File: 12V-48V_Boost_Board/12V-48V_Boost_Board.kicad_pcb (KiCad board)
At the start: 2 copper layers, 65.1 x 76.7 mm, 39 parts, among them J1 12V Input, J2 Input Current Sensing, J3 Output Current Sensing, J4 48V Output, J5 Output Measuring, Q1 FDWS86068-F085

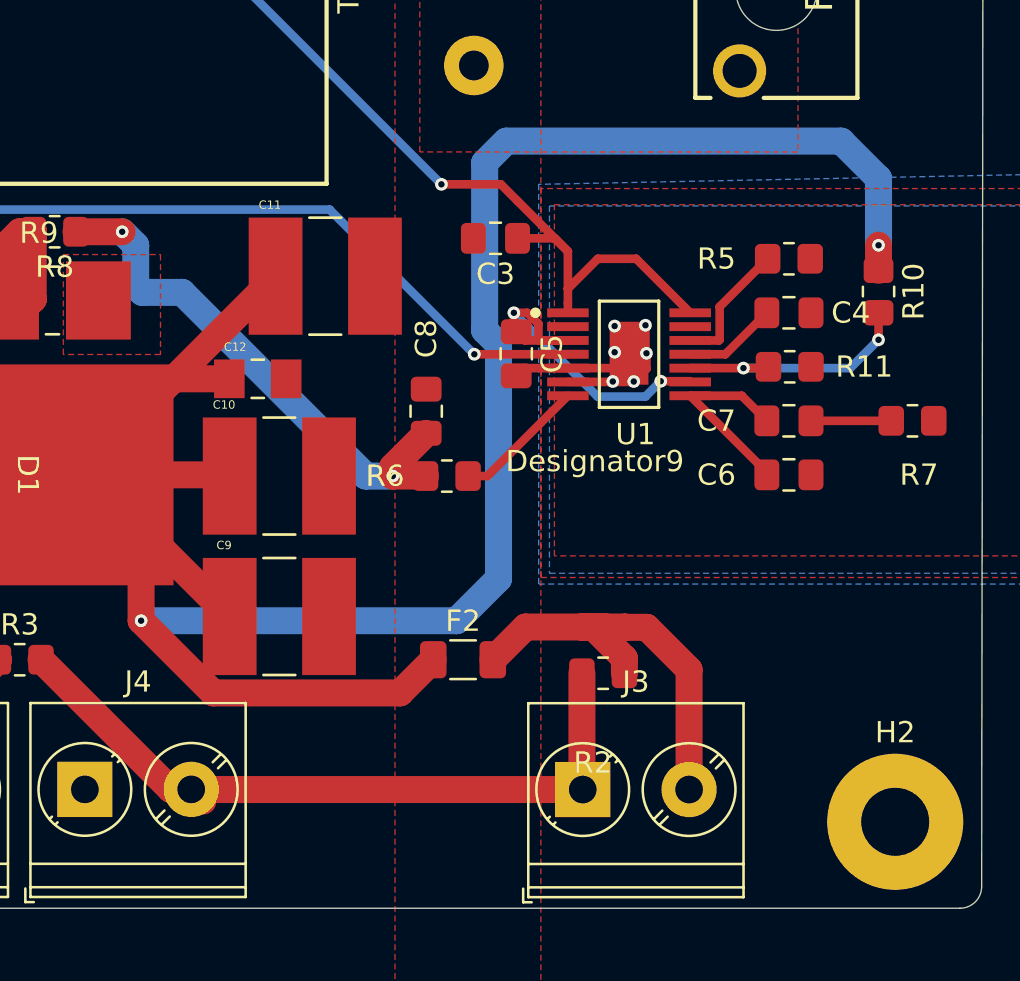
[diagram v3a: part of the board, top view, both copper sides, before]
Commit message: Added opamp
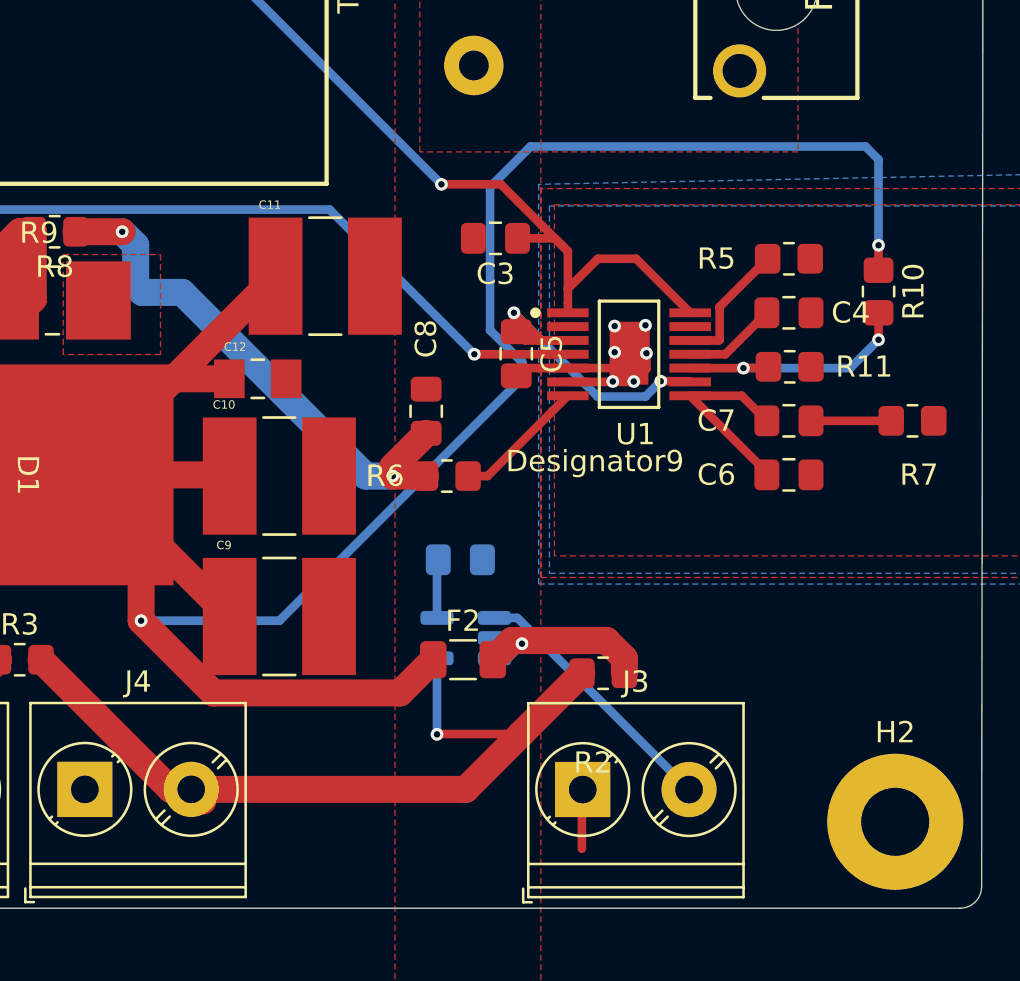
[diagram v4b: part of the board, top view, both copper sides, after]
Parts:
- added C13: 0.1uF, Capacitor_SMD:C_0805_2012Metric_Pad1.18x1.45mm_HandSolder, B.Cu at (147.2, 128.4)
- added H5: Logo, 12/48 boost:Logo_SilkScreen_10mm, B.Cu at (112.5, 93.6)
- added U2: INA180, Package_TO_SOT_SMD:SOT-23-5_HandSoldering, B.Cu at (147.4, 132.1)
- R2: value 1mΩ -> 25mΩ
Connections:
- F2 pad 2: Net-(J3-Pin_2) -> Net-(U2-IN+)
- J3 pad 1: Net-(J3-Pin_1) -> GND
- J4 pad 2: Net-(J3-Pin_1) -> Net-(J4-Pin_2)
- R2 pad 1: Net-(J3-Pin_2) -> Net-(U2-IN+)
- R2 pad 2: Net-(J3-Pin_1) -> Net-(J4-Pin_2)
- R3 pad 2: Net-(J3-Pin_1) -> Net-(J4-Pin_2)
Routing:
- net Net-(J4-Pin_2): track 0.00 -> 38.5 mm, vias 0 -> 1
- net Net-(J3-Pin_1): track 34.3 -> 0.00 mm
- net Net-(U2-IN+): track 0.00 -> 10.9 mm, vias 0 -> 1
- net Net-(J3-Pin_2): track 20.8 -> 13.1 mm
- net /Boost_Board_Chip/48V_OUTPUT: track 125.2 -> 120.6 mm
- net GND: track 16.5 -> 19.4 mm
- net +5V: track 0.00 -> 2.76 mm
- net /Boost_Board_Chip/DITHOFF: track 17.3 -> 18.2 mm
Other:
- board text added: "12V-48V BOOST BOARD KOBY SEELIGSOHN"

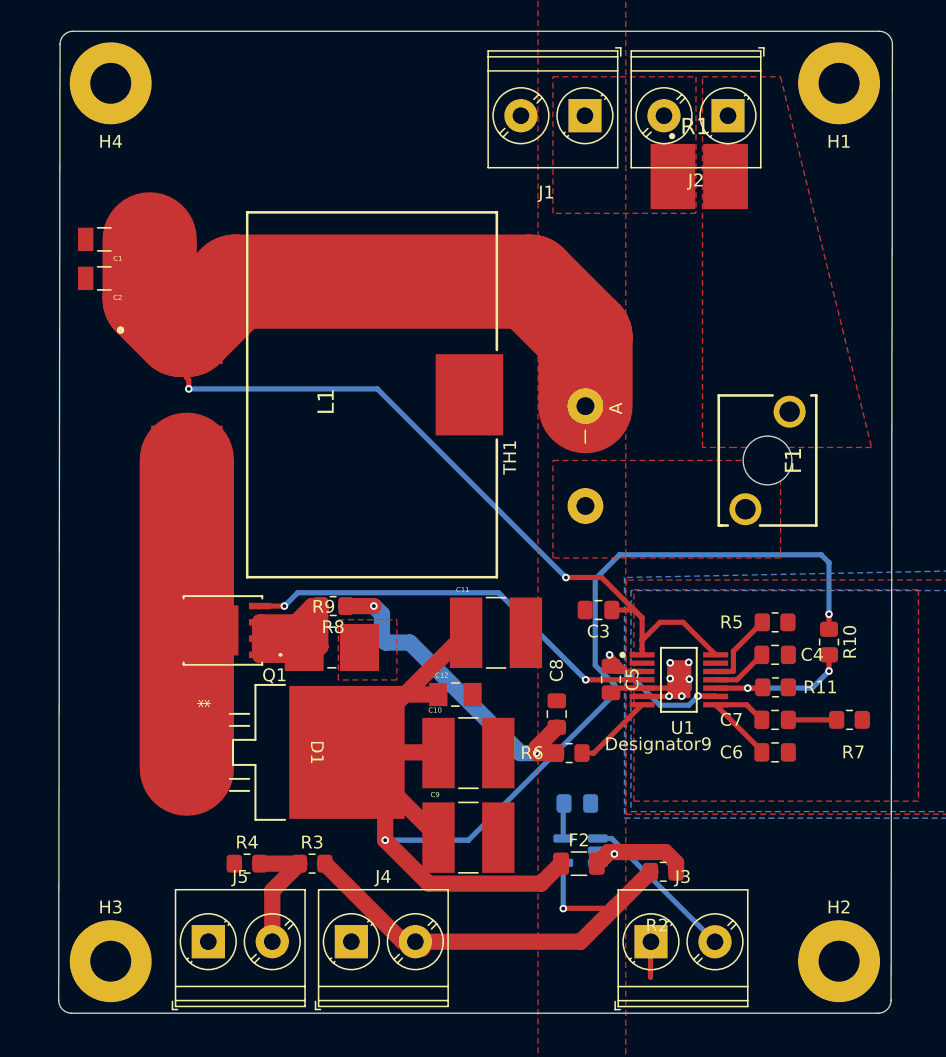
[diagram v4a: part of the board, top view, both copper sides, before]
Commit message: Changed silkscreen and vias
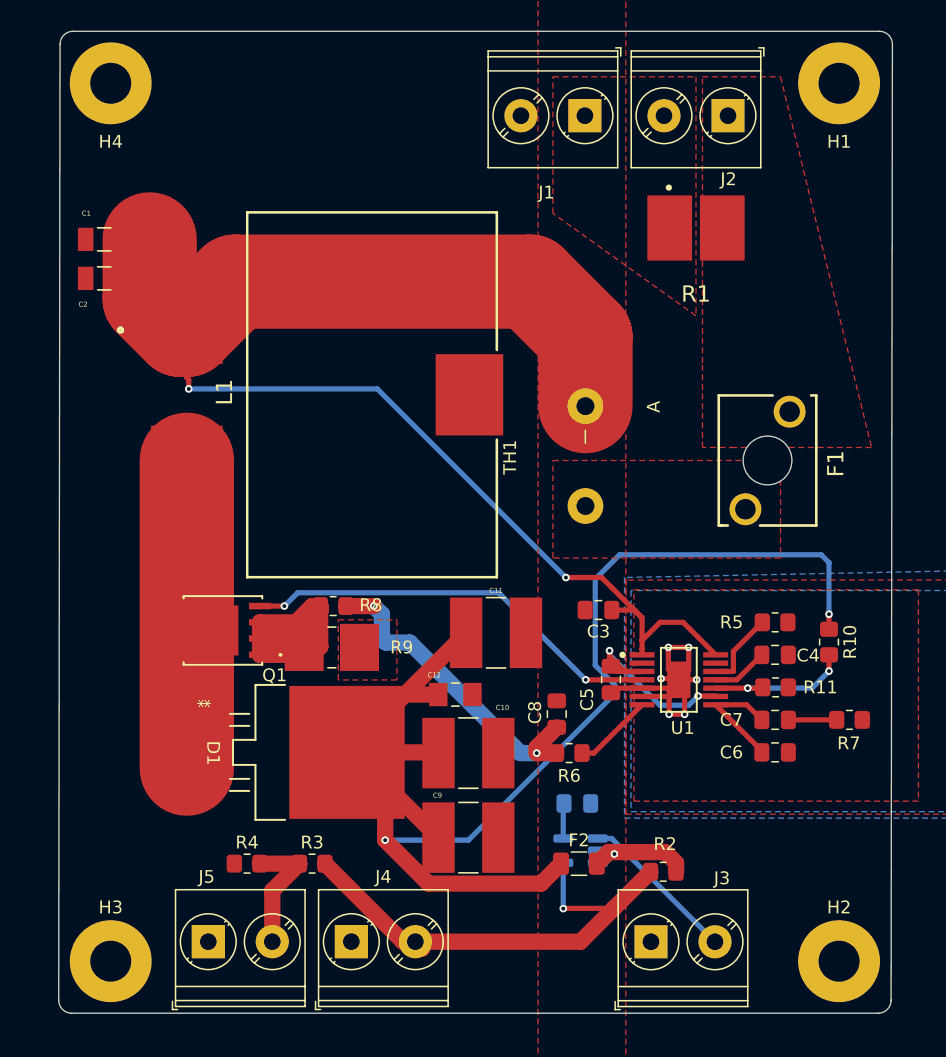
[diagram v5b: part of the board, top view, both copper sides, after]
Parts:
- moved R1 4.03 mm to (156.5, 83.4)
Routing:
- net GND: track 19.4 -> 23.8 mm

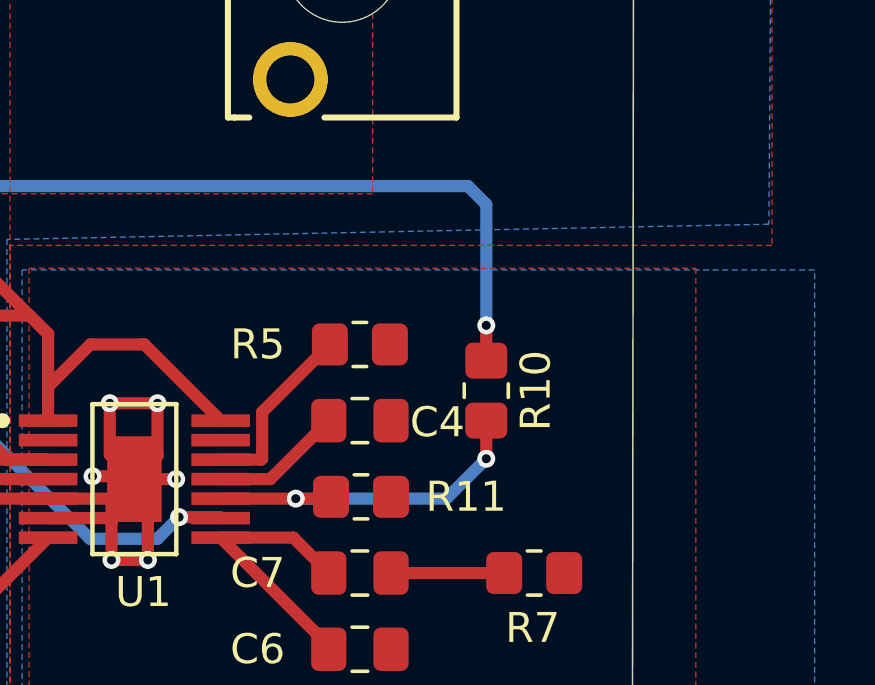
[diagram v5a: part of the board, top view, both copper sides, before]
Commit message: Changed 63nF cap footprint
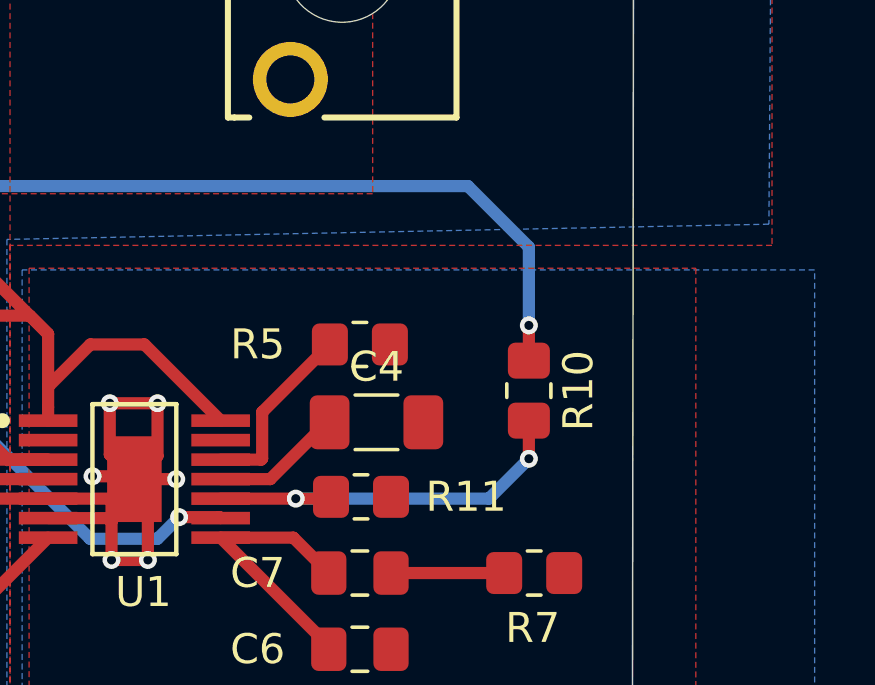
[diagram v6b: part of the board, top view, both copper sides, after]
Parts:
- C4: footprint Capacitor_SMD:C_0805_2012Metric_Pad1.18x1.45mm_HandSolder -> Capacitor_SMD:C_1206_3216Metric_Pad1.33x1.80mm_HandSolder
- F1: value 15A -> 12A
- U2: value INA180 -> INA290
- moved R10 1.42 mm to (168.3, 115.8)
- moved C4 0.56 mm to (163.2, 116.8)
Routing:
- net Net-(U1-FB): track 11.8 -> 13.2 mm
- net /Boost_Board_Chip/48V_OUTPUT: track 120.6 -> 121.1 mm
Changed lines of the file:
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@@
 			)
 		)
-		(property "Description" "08053C104KAT2A"
+		(property "Description" "CKG57NX7R2A106M500JH"
 			(at 0 0 0)
 			(layer "F.Fab")
@@
 			)
 		)
-		(property "Description" "08053C104KAT2A"
+		(property "Description" "CKG57NX7R2A106M500JH"
 			(at 0 0 0)
 			(layer "F.Fab")
@@
 			)
 		)
-		(property "Description" "08053C104KAT2A"
+		(property "Description" "CKG57NX7R2A106M500JH"
 			(at 0 0 0)
 			(layer "F.Fab")
@@
 			)
 		)
-		(property "Description" "Unpolarized capacitor"
+		(property "Description" "C3216X7R2A105M160AA"
 			(at 0 0 0)
 			(layer "F.Fab")
@@
 		)
 	)
-	(footprint "Capacitor_SMD:C_0805_2012Metric_Pad1.18x1.45mm_HandSolder"
+	(footprint "Capacitor_SMD:C_1206_3216Metric_Pad1.33x1.80mm_HandSolder"
 		(layer "F.Cu")
-		(at 162.642502 116.7842)
-		(descr "Capacitor SMD 0805 (2012 Metric), square (rectangular) end terminal, IPC_7351 nominal with elongated pad for handsoldering. (Body size source: IPC-SM-782 page 76, https://www.pcb-3d.com/wordpress/wp-content/uploads/ipc-sm-782a_amendment_1_and_2.pdf, https://docs.google.com/spreadsheets/d/1BsfQQcO9C6DZCsRaXUlFlo91Tg2WpOkGARC1WS5S8t0/edit?usp=sharing), generated with kicad-footprint-generator")
+		(at 163.195 116.84)
+		(descr "Capacitor SMD 1206 (3216 Metric), square (rectangular) end terminal, IPC_7351 nominal with elongated pad for handsoldering. (Body size source: IPC-SM-782 page 76, https://www.pcb-3d.com/wordpress/wp-content/uploads/ipc-sm-782a_amendment_1_and_2.pdf), generated with kicad-footprint-generator")
 		(tags "capacitor handsolder")
 		(property "Reference" "C4"
-			(at 2.584498 0.0558 0)
+			(at 0 -1.85 0)
 			(layer "F.SilkS")
 			(effects
@@
 		)
 		(property "Value" "63nF"
-			(at 0.2755 1.981851 0)
+			(at 0 1.85 0)
 			(layer "F.Fab")
 			(effects
@@
 			)
 		)
-		(property "Footprint" "Capacitor_SMD:C_0805_2012Metric_Pad1.18x1.45mm_HandSolder"
+		(property "Footprint" "Capacitor_SMD:C_1206_3216Metric_Pad1.33x1.80mm_HandSolder"
 			(at 0 0 0)
 			(unlocked yes)
@@
 		(attr smd)
 		(fp_line
-			(start -0.261252 -0.735)
-			(end 0.261252 -0.735)
+			(start -0.711252 -0.91)
+			(end 0.711252 -0.91)
 			(stroke
 				(width 0.12)
@@
 		)
 		(fp_line
-			(start -0.261252 0.735)
-			(end 0.261252 0.735)
+			(start -0.711252 0.91)
+			(end 0.711252 0.91)
 			(stroke
 				(width 0.12)
@@
 		)
 		(fp_line
-			(start -1.88 -0.98)
-			(end 1.88 -0.98)
+			(start -2.48 -1.15)
+			(end 2.48 -1.15)
 			(stroke
 				(width 0.05)
@@
 		)
 		(fp_line
-			(start -1.88 0.98)
-			(end -1.88 -0.98)
+			(start -2.48 1.15)
+			(end -2.48 -1.15)
 			(stroke
 				(width 0.05)
@@
 		)
 		(fp_line
-			(start 1.88 -0.98)
-			(end 1.88 0.98)
+			(start 2.48 -1.15)
+			(end 2.48 1.15)
 			(stroke
 				(width 0.05)
@@
 		)
 		(fp_line
-			(start 1.88 0.98)
-			(end -1.88 0.98)
+			(start 2.48 1.15)
+			(end -2.48 1.15)
 			(stroke
 				(width 0.05)
@@
 		)
 		(fp_line
-			(start -1 -0.625)
-			(end 1 -0.625)
+			(start -1.6 -0.8)
+			(end 1.6 -0.8)
 			(stroke
 				(width 0.1)
@@
 		)
 		(fp_line
-			(start -1 0.625)
-			(end -1 -0.625)
+			(start -1.6 0.8)
+			(end -1.6 -0.8)
 			(stroke
 				(width 0.1)
@@
 		)
 		(fp_line
-			(start 1 -0.625)
-			(end 1 0.625)
+			(start 1.6 -0.8)
+			(end 1.6 0.8)
 			(stroke
 				(width 0.1)
@@
 		)
 		(fp_line
-			(start 1 0.625)
-			(end -1 0.625)
+			(start 1.6 0.8)
+			(end -1.6 0.8)
 			(stroke
 				(width 0.1)
@@
 			(effects
 				(font
-					(size 0.5 0.5)
-					(thickness 0.08)
+					(size 0.8 0.8)
+					(thickness 0.12)
 				)
 			)
 		)
 		(pad "1" smd roundrect
-			(at -1.0375 0)
-			(size 1.175 1.45)
+			(at -1.5625 0)
+			(size 1.325 1.8)
 			(layers "F.Cu" "F.Paste" "F.Mask")
-			(roundrect_rratio 0.212766)
+			(roundrect_rratio 0.188679)
 			(net 3 "Net-(U1-SS)")
 			(pintype "passive")
 		)
 		(pad "2" smd roundrect
-			(at 1.0375 0)
-			(size 1.175 1.45)
+			(at 1.5625 0)
+			(size 1.325 1.8)
 			(layers "F.Cu" "F.Paste" "F.Mask")
-			(roundrect_rratio 0.212766)
+			(roundrect_rratio 0.188679)
 			(net 2 "GND")
 			(pintype "passive")
 		)
-		(model "${KICAD8_3DMODEL_DIR}/Capacitor_SMD.3dshapes/C_0805_2012Metric.wrl"
+		(model "${KICAD8_3DMODEL_DIR}/Capacitor_SMD.3dshapes/C_1206_3216Metric.wrl"
 			(offset
 				(xyz 0 0 0)
@@
 	(footprint "Resistor_SMD:R_0805_2012Metric_Pad1.20x1.40mm_HandSolder"
 		(layer "F.Cu")
-		(at 166.855002 115.7842 -90)
+		(at 168.275 115.7842 -90)
 		(descr "Resistor SMD 0805 (2012 Metric), square (rectangular) end terminal, IPC_7351 nominal with elongated pad for handsoldering. (Body size source: IPC-SM-782 page 72, https://www.pcb-3d.com/wordpress/wp-content/uploads/ipc-sm-782a_amendment_1_and_2.pdf), generated with kicad-footprint-generator")
 		(tags "resistor handsolder")
@@
 			)
 		)
-		(property "Value" "15A"
+		(property "Value" "12A"
 			(at 3.81 -0.303 90)
 			(layer "F.SilkS")
@@
 			)
 		)
-		(property "Value" "INA180"
+		(property "Value" "INA290"
 			(at 0 -2.9 0)
 			(layer "B.Fab")
@@
 		)
 		(height 20.828)
-		(gr_text "2700.0000 mils"
+		(gr_text "68.5800 mm"
 			(at 88.116 106.426 90)
 			(layer "F.Cu")
@@
 	)
 	(segment
-		(start 166.855002 113.6092)
-		(end 166.855002 114.7842)
+		(start 168.275 113.6092)
+		(end 168.275 114.7842)
 		(width 0.4064)
 		(layer "F.Cu")
@@
 	)
 	(via
-		(at 166.855002 113.6092)
+		(at 168.275 113.6092)
 		(size 0.6)
 		(drill 0.3)
@@
 	)
 	(segment
-		(start 166.243 108.966)
-		(end 150.495 108.966)
+		(start 148.59 110.871)
+		(end 148.59 117.602)
 		(width 0.4064)
 		(layer "B.Cu")
@@
 	)
 	(segment
-		(start 166.855002 109.578002)
-		(end 166.243 108.966)
+		(start 148.59 117.602)
+		(end 150.114 119.126)
 		(width 0.4064)
 		(layer "B.Cu")
@@
 	)
 	(segment
-		(start 166.855002 113.6092)
-		(end 166.855002 109.578002)
+		(start 168.275 110.998)
+		(end 166.243 108.966)
 		(width 0.4064)
 		(layer "B.Cu")
@@
 	)
 	(segment
-		(start 150.114 119.126)
-		(end 150.114 119.836762)
+		(start 138.688562 131.2622)
+		(end 132.184002 131.2622)
 		(width 0.4064)
 		(layer "B.Cu")
@@
 	)
 	(segment
-		(start 148.59 117.602)
-		(end 150.114 119.126)
+		(start 150.114 119.126)
+		(end 150.114 119.836762)
 		(width 0.4064)
 		(layer "B.Cu")
@@
 	)
 	(segment
-		(start 138.688562 131.2622)
-		(end 132.184002 131.2622)
+		(start 166.243 108.966)
+		(end 150.495 108.966)
 		(width 0.4064)
 		(layer "B.Cu")
@@
 	)
 	(segment
-		(start 148.59 110.871)
-		(end 148.59 117.602)
+		(start 168.275 113.6092)
+		(end 168.275 110.998)
 		(width 0.4064)
 		(layer "B.Cu")
@@
 	)
 	(segment
-		(start 166.855002 118.0542)
-		(end 166.855002 116.7842)
+		(start 168.275 118.0542)
+		(end 168.275 116.7842)
 		(width 0.4064)
 		(layer "F.Cu")
@@
 	)
 	(via
-		(at 166.855002 118.0542)
+		(at 168.275 118.0542)
 		(size 0.6)
 		(drill 0.3)
@@
 	)
 	(segment
-		(start 165.525 119.384202)
-		(end 166.855002 118.0542)
+		(start 166.944998 119.384202)
+		(end 168.275 118.0542)
 		(width 0.4064)
 		(layer "B.Cu")
@@
 	(segment
 		(start 160.505002 119.384202)
-		(end 165.525 119.384202)
+		(end 166.944998 119.384202)
 		(width 0.4064)
 		(layer "B.Cu")
